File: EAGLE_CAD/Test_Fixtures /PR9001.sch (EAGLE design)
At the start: 9 parts, among them T10 PR9001_TESTPOINT, T11 PR9001_TESTPOINT, T12 PR9001_TESTPOINT, T13 PR9001_TESTPOINT, T2 PR9001_TESTPOINT, T3 PR9001_TESTPOINT, T4 PR9001_TESTPOINT, T5 PR9001_TESTPOINT

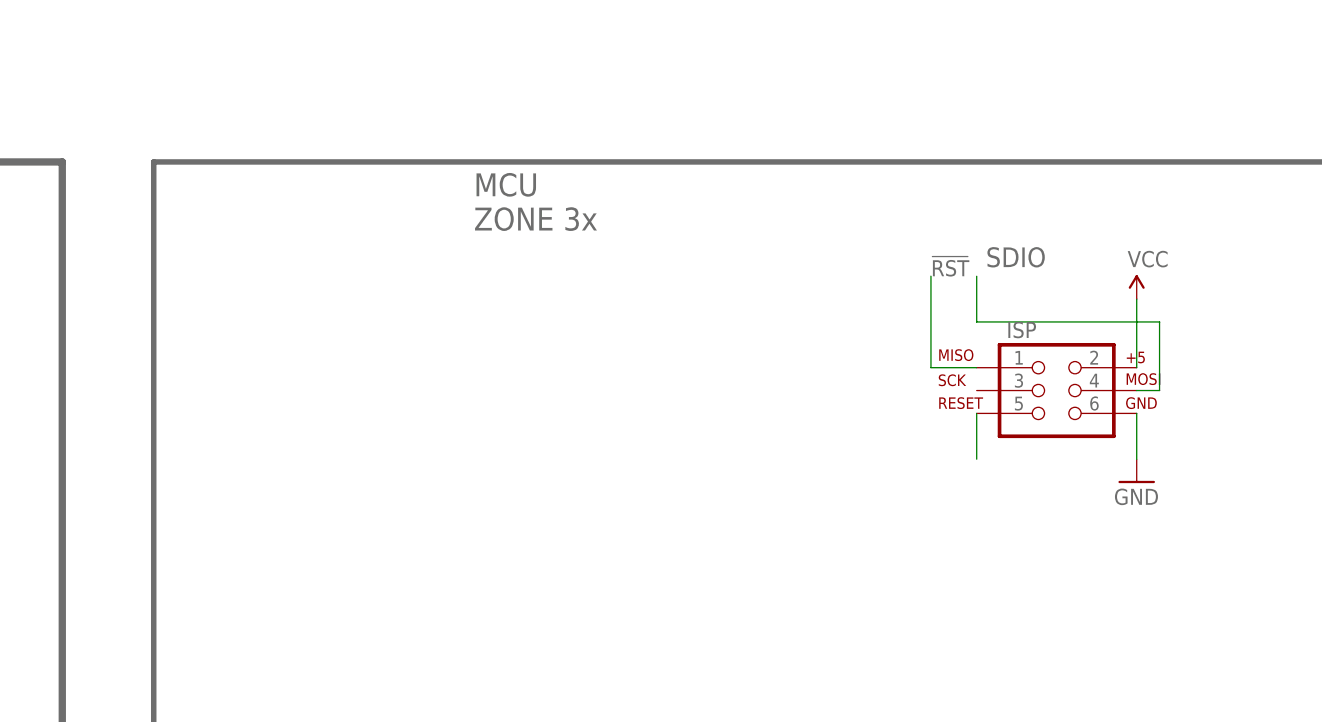
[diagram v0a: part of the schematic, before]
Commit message: PR9001
added pass / fail LEDs
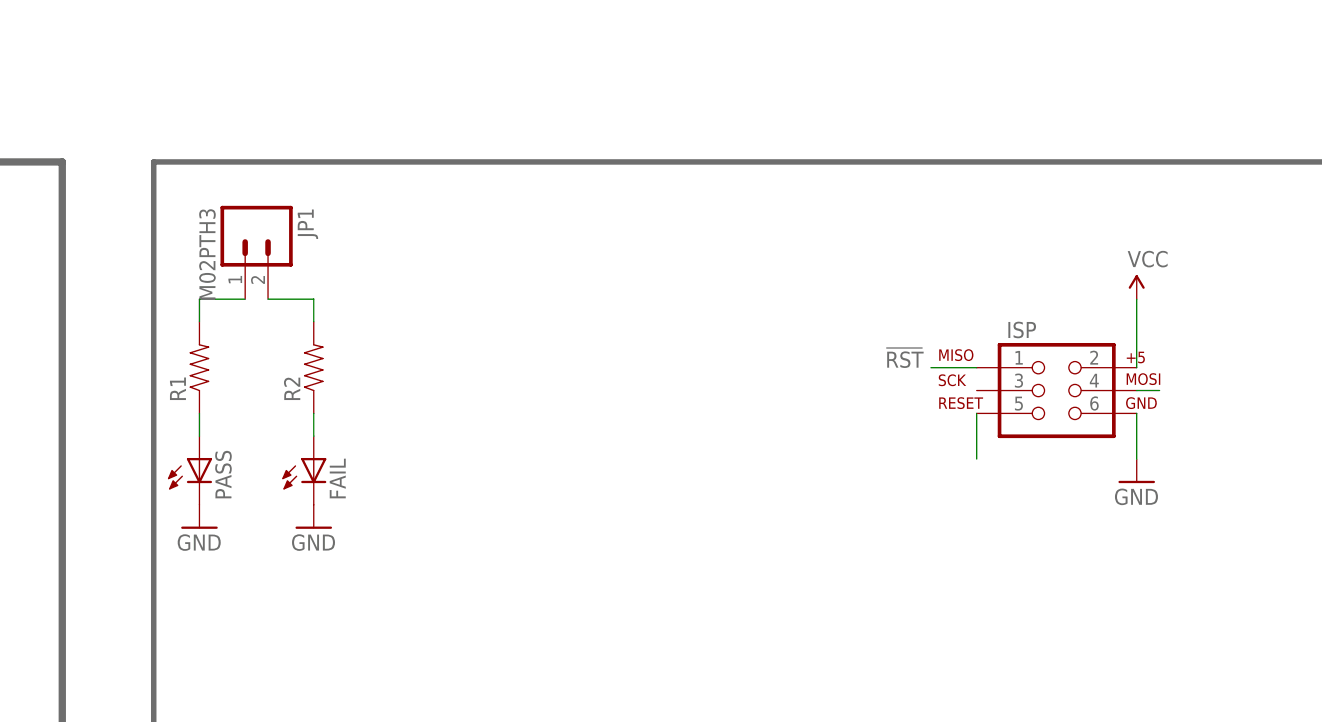
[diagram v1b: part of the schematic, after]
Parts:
- added FAIL, PASS: (no value), adafruit:LED5MM
- added JP1: M02PTH3, SparkFun-Connectors:M02PTH3
- added R1, R2: (no value), SparkFun-Resistors:RESISTORPTH-1/4W-VERT
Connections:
- new net N$1: JP1.2, R2.2
- new net N$2: PASS.A, R1.1
- new net N$3: JP1.1, R1.2
- new net N$4: FAIL.A, R2.1
- net GND: now also FAIL.C, PASS.C
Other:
- note removed: "MCU ZONE 3x"
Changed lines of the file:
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@@
 <part name="T12" library="PR_Parts_Library" deviceset="PR9001_TESTPOINT" device=""/>
 <part name="T13" library="PR_Parts_Library" deviceset="PR9001_TESTPOINT" device=""/>
+<part name="PASS" library="adafruit" deviceset="LED" device="5MM"/>
+<part name="FAIL" library="adafruit" deviceset="LED" device="5MM"/>
+<part name="JP1" library="SparkFun-Connectors" deviceset="M02" device="PTH3"/>
+<part name="R1" library="SparkFun-Resistors" deviceset="RESISTOR" device="PTH-1/4W-VERT"/>
+<part name="R2" library="SparkFun-Resistors" deviceset="RESISTOR" device="PTH-1/4W-VERT"/>
+<part name="GND1" library="SparkFun-Aesthetics" deviceset="GND" device=""/>
+<part name="GND2" library="SparkFun-Aesthetics" deviceset="GND" device=""/>
 </parts>
 <sheets>
@@
 <wire x1="269.24" y1="152.4" x2="269.24" y2="88.9" width="0.6096" layer="96"/>
 <wire x1="269.24" y1="88.9" x2="121.92" y2="88.9" width="0.6096" layer="96"/>
-<text x="157.48" y="144.78" size="2.54" layer="96">MCU
-ZONE 3x</text>
 <text x="-27.94" y="162.56" size="3.81" layer="96">PUBLIC RADIO PR9023
 Production Board </text>
@@
 <instance part="T12" gate="G$1" x="86.36" y="109.22"/>
 <instance part="T13" gate="G$1" x="96.52" y="109.22"/>
+<instance part="PASS" gate="G$1" x="127" y="119.38"/>
+<instance part="FAIL" gate="G$1" x="139.7" y="119.38"/>
+<instance part="JP1" gate="G$1" x="132.08" y="144.78" rot="R270"/>
+<instance part="R1" gate="G$1" x="127" y="129.54" rot="R90"/>
+<instance part="R2" gate="G$1" x="139.7" y="129.54" rot="R90"/>
+<instance part="GND1" gate="1" x="139.7" y="111.76"/>
+<instance part="GND2" gate="1" x="127" y="111.76"/>
 </instances>
 <busses>
@@
 <pinref part="GND14" gate="1" pin="GND"/>
 </segment>
+<segment>
+<pinref part="FAIL" gate="G$1" pin="C"/>
+<pinref part="GND1" gate="1" pin="GND"/>
+</segment>
+<segment>
+<pinref part="PASS" gate="G$1" pin="C"/>
+<pinref part="GND2" gate="1" pin="GND"/>
+</segment>
 </net>
 <net name="!RST" class="0">
@@
 <pinref part="ISP" gate="G$1" pin="1"/>
 <wire x1="208.28" y1="129.54" x2="213.36" y2="129.54" width="0.1524" layer="91"/>
-<wire x1="208.28" y1="129.54" x2="208.28" y2="139.7" width="0.1524" layer="91"/>
-<label x="208.28" y="139.7" size="1.778" layer="95"/>
+<label x="203.2" y="129.54" size="1.778" layer="95"/>
 </segment>
 <segment>
@@
 <net name="SDIO" class="0">
 <segment>
-<wire x1="233.68" y1="134.62" x2="233.68" y2="127" width="0.1524" layer="91"/>
 <pinref part="ISP" gate="G$1" pin="4"/>
 <wire x1="233.68" y1="127" x2="231.14" y2="127" width="0.1524" layer="91"/>
-<label x="214.376" y="140.716" size="2.1844" layer="95"/>
-<wire x1="233.68" y1="134.62" x2="213.36" y2="134.62" width="0.1524" layer="91"/>
-<wire x1="213.36" y1="134.62" x2="213.36" y2="139.7" width="0.1524" layer="91"/>
 </segment>
 <segment>
@@
 </segment>
 </net>
+<net name="N$2" class="0">
+<segment>
+<pinref part="R1" gate="G$1" pin="1"/>
+<pinref part="PASS" gate="G$1" pin="A"/>
+<wire x1="127" y1="121.92" x2="127" y2="124.46" width="0.1524" layer="91"/>
+</segment>
+</net>
+<net name="N$4" class="0">
+<segment>
+<pinref part="R2" gate="G$1" pin="1"/>
+<pinref part="FAIL" gate="G$1" pin="A"/>
+<wire x1="139.7" y1="121.92" x2="139.7" y2="124.46" width="0.1524" layer="91"/>
+</segment>
+</net>
+<net name="N$1" class="0">
+<segment>
+<pinref part="JP1" gate="G$1" pin="2"/>
+<wire x1="134.62" y1="137.16" x2="139.7" y2="137.16" width="0.1524" layer="91"/>
+<pinref part="R2" gate="G$1" pin="2"/>
+<wire x1="139.7" y1="137.16" x2="139.7" y2="134.62" width="0.1524" layer="91"/>
+</segment>
+</net>
+<net name="N$3" class="0">
+<segment>
+<pinref part="JP1" gate="G$1" pin="1"/>
+<wire x1="132.08" y1="137.16" x2="127" y2="137.16" width="0.1524" layer="91"/>
+<pinref part="R1" gate="G$1" pin="2"/>
+<wire x1="127" y1="137.16" x2="127" y2="134.62" width="0.1524" layer="91"/>
+</segment>
+</net>
